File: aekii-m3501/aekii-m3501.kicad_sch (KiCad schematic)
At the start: 2 parts, among them J1 5749181-1, J2 Conn_01x04

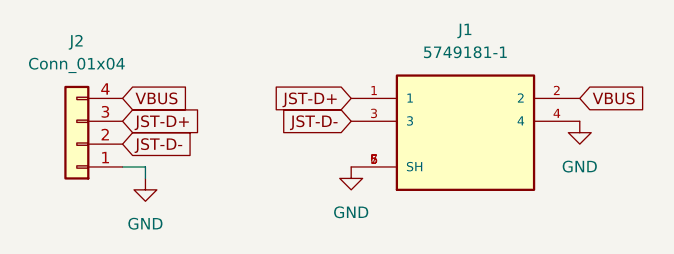
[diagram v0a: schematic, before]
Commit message: Renamed ADB connector
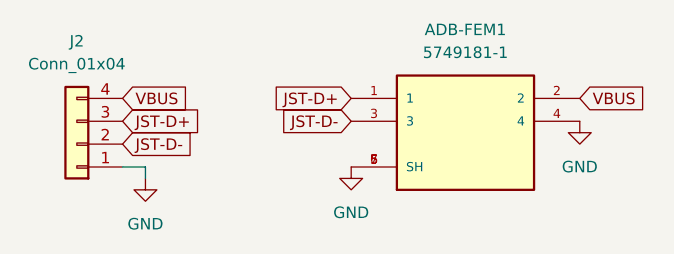
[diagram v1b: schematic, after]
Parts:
- renumbered J1 to ADB-FEM1
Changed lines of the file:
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@@
   (symbol (lib_id "ADB:5749181-1") (at 67.31 27.94 0) (unit 1)
     (in_bom yes) (on_board yes) (dnp no) (fields_autoplaced)
-    (property "Reference" "J1" (at 67.31 17.78 0)
+    (property "Reference" "ADB-FEM1" (at 67.31 17.78 0)
       (effects (font (size 1.27 1.27)))
     )
@@
       (project "aekii-m3501"
         (path "/10fa40d7-dfa7-4104-a535-2d62cfab9a1c"
-          (reference "J1") (unit 1)
+          (reference "ADB-FEM1") (unit 1)
         )
       )

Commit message: switched D+/D- on USB PCB, isolated shield from ground
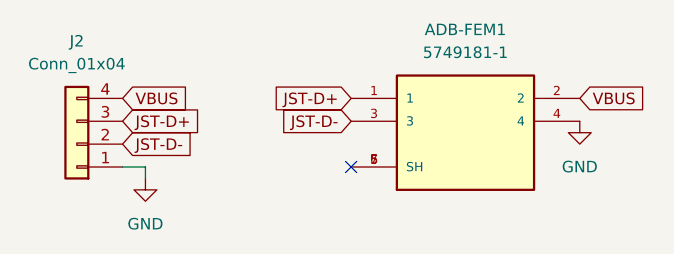
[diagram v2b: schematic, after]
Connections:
- net GND: no longer ADB-FEM1.5 (SH), ADB-FEM1.6 (SH), ADB-FEM1.7 (SH)
- new net: ADB-FEM1.5 (SH), ADB-FEM1.6 (SH), ADB-FEM1.7 (SH)
- no-connect marks 0 -> 1
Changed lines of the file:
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@@
 (kicad_sch (version 20230121) (generator eeschema)
   (paper "A4")
+  (no_connect (at 54.61 33.02))
   (wire (pts (xy 29.21 33.02) (xy 31.75 33.02))
     (stroke (width 0) (type default))
@@
         )
       )
-    )
-  )
-  (symbol (lib_id "power:GND") (at 54.61 33.02 0) (unit 1)
-    (in_bom yes) (on_board yes) (dnp no) (fields_autoplaced)
-    (property "Reference" "#PWR02" (at 54.61 39.37 0)
-      (effects (font (size 1.27 1.27)) hide)
-    )
-    (property "Value" "GND" (at 54.61 38.1 0)
-      (effects (font (size 1.27 1.27)))
-    )
-    (property "Footprint" "" (at 54.61 33.02 0)
-      (effects (font (size 1.27 1.27)) hide)
-    )
-    (property "Datasheet" "" (at 54.61 33.02 0)
-      (effects (font (size 1.27 1.27)) hide)
-    )
-    (pin "1")
-    (instances
-      (project "aekii-m3501"
-        (path "/10fa40d7-dfa7-4104-a535-2d62cfab9a1c"
-          (reference "#PWR02") (unit 1)
-        )
-      )
